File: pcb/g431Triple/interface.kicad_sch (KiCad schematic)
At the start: 29 parts, among them P4 har-flexicon 2,54 MSH-4, P5 har-flexicon 2,54 MSH-4, P6 har-flexicon 2,54 MSH-4, P7 WAGO2061-602, P8 WAGO2061-602, P9 WAGO2061-602, U4 SP3485CN, U5 SP3485CN, U6 SP3485CN

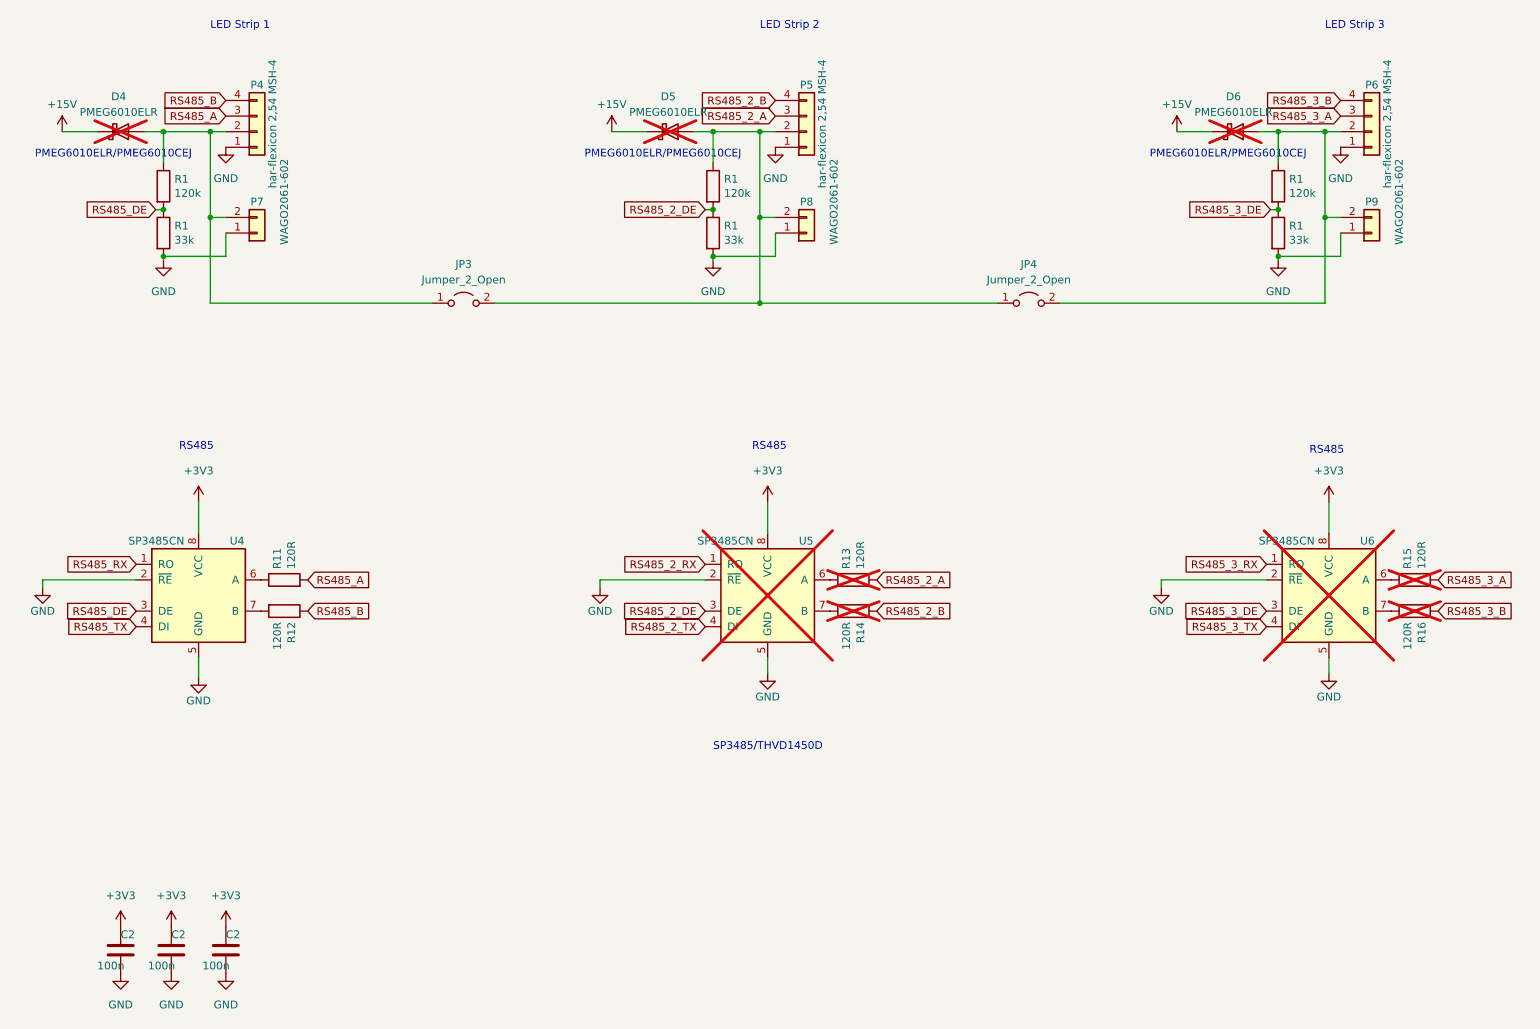
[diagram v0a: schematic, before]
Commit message: Rename to g431/g431Triple, new pin ordering for Harting connector
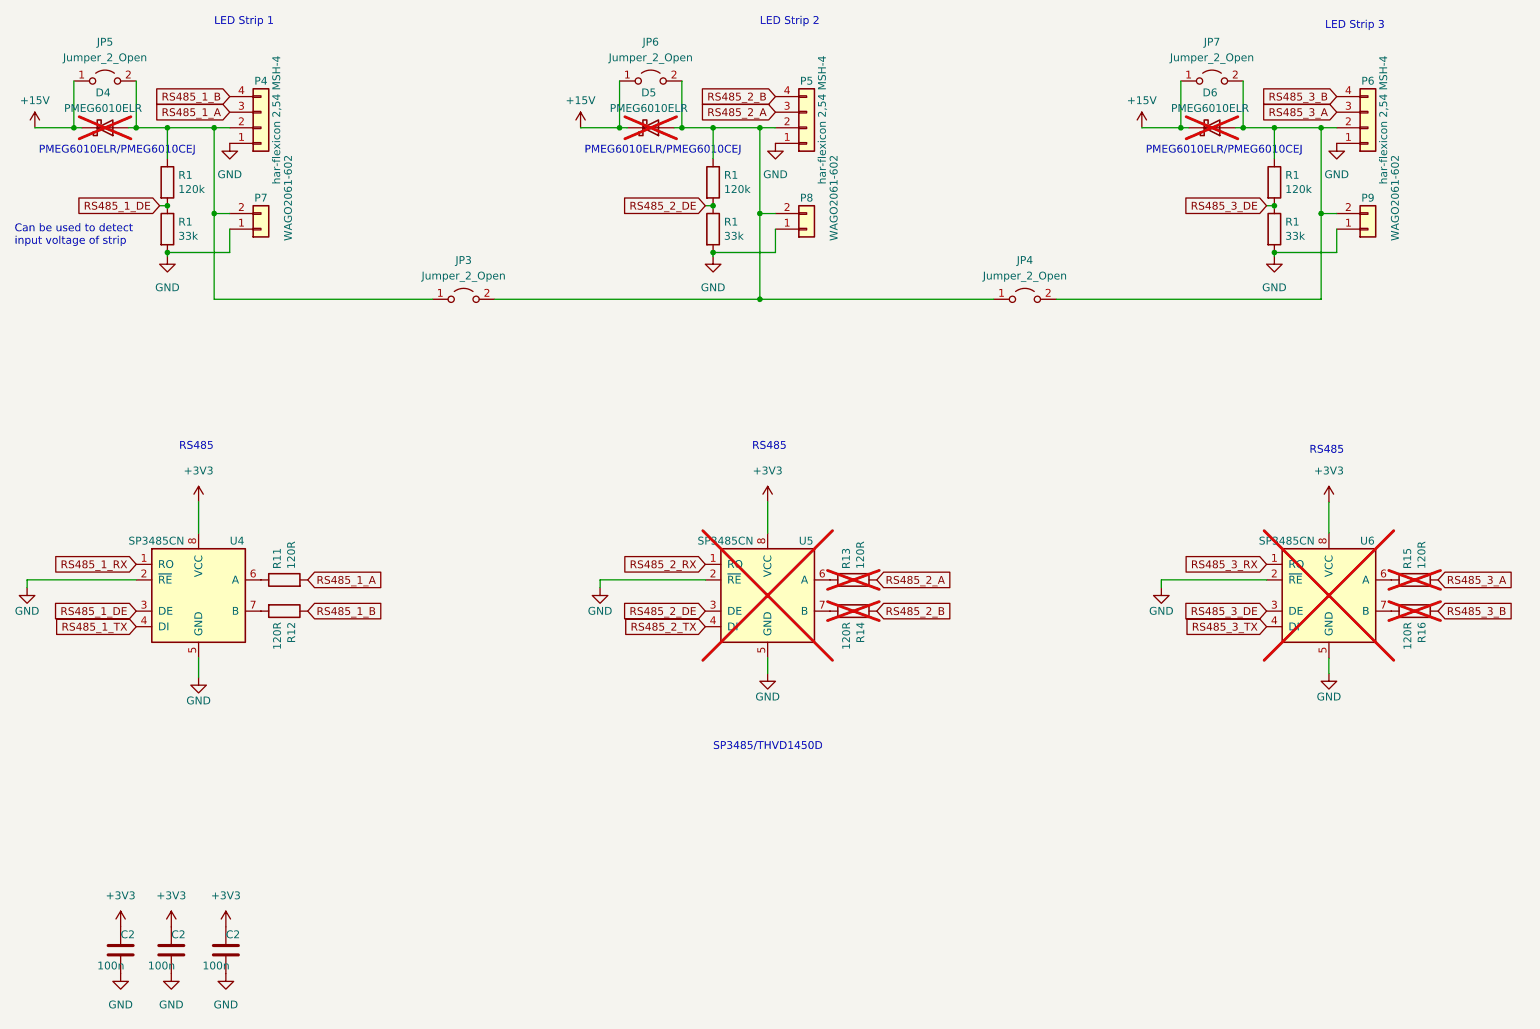
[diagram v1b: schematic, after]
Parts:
- added JP5, JP6, JP7: Jumper_2_Open, local:Jumper, symbol Jumper:Jumper_2_Open
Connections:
- net +15V: now also JP5.1 (A), JP6.1 (A), JP7.1 (A)
- net at D5.2 (A), JP3.2 (B), JP4.1 (A)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: now also JP6.2 (B)
- net at D6.2 (A), JP4.2 (B), P6.2 (Pin_2)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: now also JP7.2 (B)
- net at D4.2 (A), JP3.1 (A), P4.2 (Pin_2)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: now also JP5.2 (B)
- net RS485_A renamed RS485_1_A
- net RS485_B renamed RS485_1_B
- net RS485_DE renamed RS485_1_DE
- net RS485_RX renamed RS485_1_RX
- net RS485_TX renamed RS485_1_TX
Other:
- note added: "Can be used to detect input voltage of strip"
- moved on the sheet: D4, D5, D6, JP3, JP4, P4, P5, P6, P7, P8, P9, R1

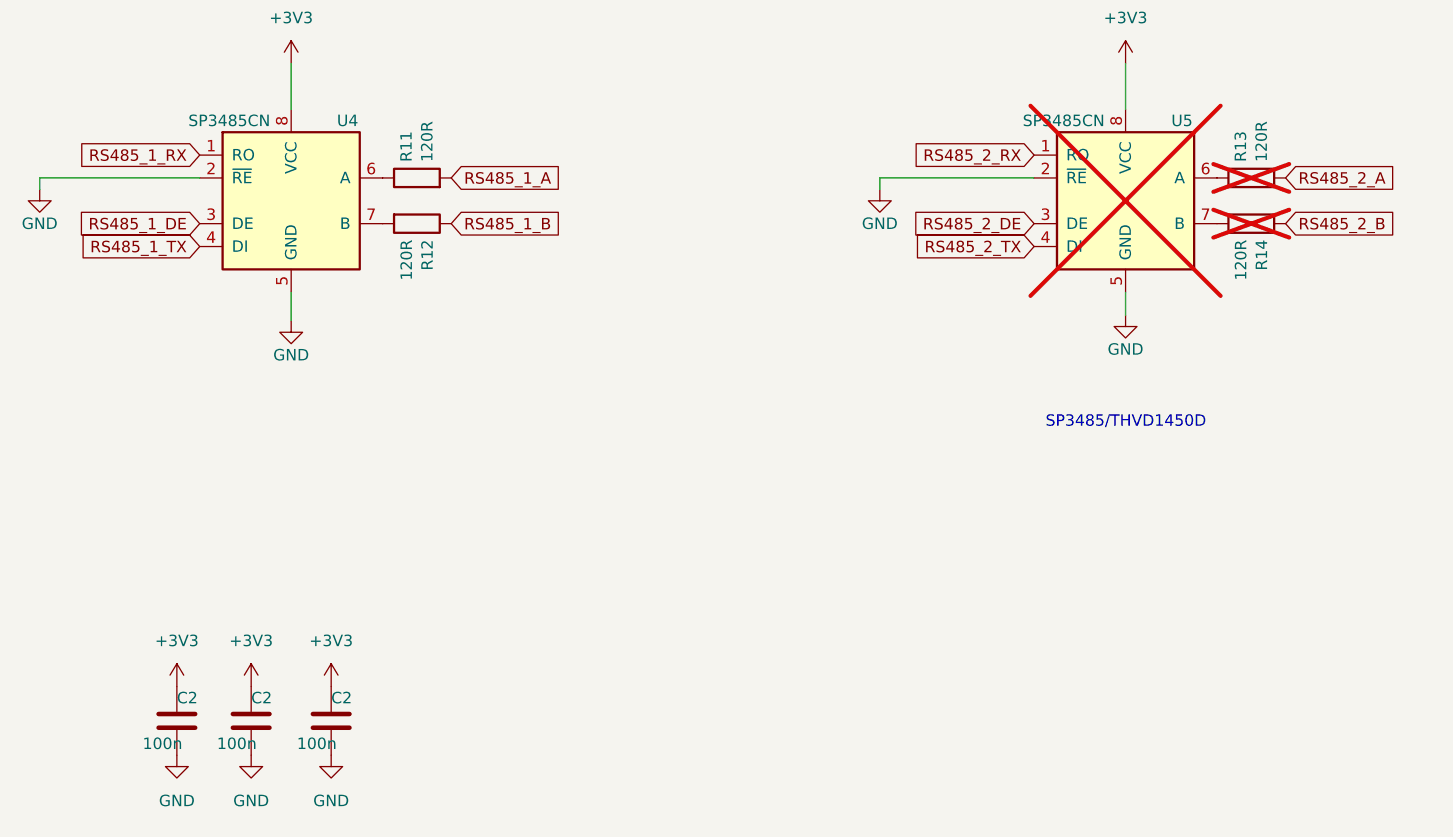
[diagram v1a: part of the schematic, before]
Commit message: Add color temperature
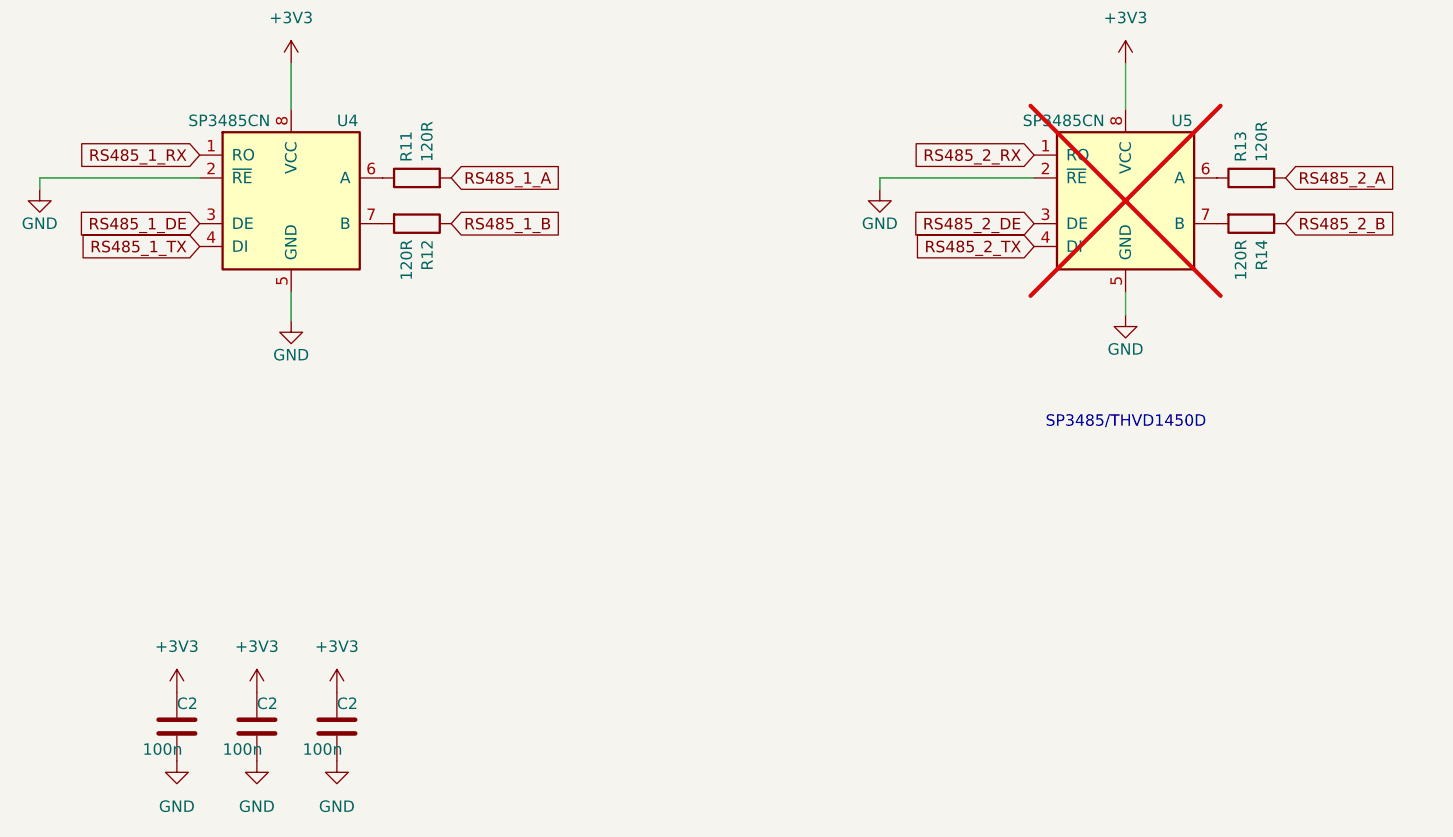
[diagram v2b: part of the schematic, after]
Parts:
- R13, R14: now fitted
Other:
- moved on the sheet: C2
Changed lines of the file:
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@@
 		(in_bom yes)
 		(on_board yes)
-		(dnp yes)
+		(dnp no)
 		(property "Reference" "R14"
 			(at 157.3784 126.238 0)
@@
 		(in_bom yes)
 		(on_board yes)
-		(dnp yes)
+		(dnp no)
 		(property "Reference" "R13"
 			(at 155.0416 117.602 0)
@@
 	(symbol
 		(lib_id "Device:C")
-		(at 45.085 179.705 0)
+		(at 45.72 180.34 0)
 		(unit 1)
 		(exclude_from_sim no)
@@
 		(dnp no)
 		(property "Reference" "C2"
-			(at 45.085 177.165 0)
+			(at 45.72 177.8 0)
 			(effects
 				(font
@@
 		)
 		(property "Value" "100n"
-			(at 41.275 182.245 0)
+			(at 41.91 182.88 0)
 			(effects
 				(font
@@
 		)
 		(property "Footprint" "local:0603"
-			(at 46.0502 183.515 0)
+			(at 46.6852 184.15 0)
 			(effects
 				(font
@@
 		)
 		(property "Datasheet" "~"
-			(at 45.085 179.705 0)
+			(at 45.72 180.34 0)
 			(effects
 				(font
@@
 		)
 		(property "Description" ""
-			(at 45.085 179.705 0)
+			(at 45.72 180.34 0)
 			(effects
 				(font
@@
 			(project "control"
 				(path "/4b540715-c4ed-4902-8525-92fb403f6b2e/20eb032d-dad8-4c28-86ad-cc4f262ed8e2"
-					(reference "C16")
+					(reference "C17")
 					(unit 1)
 				)
@@
 	(symbol
 		(lib_id "power:GND")
-		(at 53.975 183.515 0)
+		(at 54.61 184.15 0)
 		(unit 1)
 		(exclude_from_sim no)
@@
 		(fields_autoplaced yes)
 		(property "Reference" "#PWR010"
-			(at 53.975 189.865 0)
+			(at 54.61 190.5 0)
 			(effects
 				(font
@@
 		)
 		(property "Value" "GND"
-			(at 53.975 188.595 0)
+			(at 54.61 189.23 0)
 			(effects
 				(font
@@
 		)
 		(property "Footprint" ""
-			(at 53.975 183.515 0)
+			(at 54.61 184.15 0)
 			(effects
 				(font
@@
 		)
 		(property "Datasheet" ""
-			(at 53.975 183.515 0)
+			(at 54.61 184.15 0)
 			(effects
 				(font
@@
 		)
 		(property "Description" ""
-			(at 53.975 183.515 0)
+			(at 54.61 184.15 0)
 			(effects
 				(font
@@
 	(symbol
 		(lib_id "Device:C")
-		(at 36.83 179.705 0)
+		(at 36.83 180.34 0)
 		(unit 1)
 		(exclude_from_sim no)
@@
 		(dnp no)
 		(property "Reference" "C2"
-			(at 36.83 177.165 0)
+			(at 36.83 177.8 0)
 			(effects
 				(font
@@
 		)
 		(property "Value" "100n"
-			(at 33.02 182.245 0)
+			(at 33.02 182.88 0)
 			(effects
 				(font
@@
 		)
 		(property "Footprint" "local:0603"
-			(at 37.7952 183.515 0)
+			(at 37.7952 184.15 0)
 			(effects
 				(font
@@
 		)
 		(property "Datasheet" "~"
-			(at 36.83 179.705 0)
+			(at 36.83 180.34 0)
 			(effects
 				(font
@@
 		)
 		(property "Description" ""
-			(at 36.83 179.705 0)
+			(at 36.83 180.34 0)
 			(effects
 				(font
@@
 			(project "control"
 				(path "/4b540715-c4ed-4902-8525-92fb403f6b2e/20eb032d-dad8-4c28-86ad-cc4f262ed8e2"
-					(reference "C15")
+					(reference "C16")
 					(unit 1)
 				)
@@
 	(symbol
 		(lib_id "Device:C")
-		(at 53.975 179.705 0)
+		(at 54.61 180.34 0)
 		(unit 1)
 		(exclude_from_sim no)
@@
 		(dnp no)
 		(property "Reference" "C2"
-			(at 53.975 177.165 0)
+			(at 54.61 177.8 0)
 			(effects
 				(font
@@
 		)
 		(property "Value" "100n"
-			(at 50.165 182.245 0)
+			(at 50.8 182.88 0)
 			(effects
 				(font
@@
 		)
 		(property "Footprint" "local:0603"
-			(at 54.9402 183.515 0)
+			(at 55.5752 184.15 0)
 			(effects
 				(font
@@
 		)
 		(property "Datasheet" "~"
-			(at 53.975 179.705 0)
+			(at 54.61 180.34 0)
 			(effects
 				(font
@@
 		)
 		(property "Description" ""
-			(at 53.975 179.705 0)
+			(at 54.61 180.34 0)
 			(effects
 				(font
@@
 			(project "control"
 				(path "/4b540715-c4ed-4902-8525-92fb403f6b2e/20eb032d-dad8-4c28-86ad-cc4f262ed8e2"
-					(reference "C17")
+					(reference "C18")
 					(unit 1)
 				)
@@
 	(symbol
 		(lib_id "power:+3V3")
-		(at 45.085 175.895 0)
+		(at 45.72 176.53 0)
 		(unit 1)
 		(exclude_from_sim no)
@@
 		(fields_autoplaced yes)
 		(property "Reference" "#PWR09"
-			(at 45.085 179.705 0)
+			(at 45.72 180.34 0)
 			(effects
 				(font
@@
 		)
 		(property "Value" "+3V3"
-			(at 45.085 170.815 0)
+			(at 45.72 171.45 0)
 			(effects
 				(font
@@
 		)
 		(property "Footprint" ""
-			(at 45.085 175.895 0)
+			(at 45.72 176.53 0)
 			(effects
 				(font
@@
 		)
 		(property "Datasheet" ""
-			(at 45.085 175.895 0)
+			(at 45.72 176.53 0)
 			(effects
 				(font
@@
 		)
 		(property "Description" ""
-			(at 45.085 175.895 0)
+			(at 45.72 176.53 0)
 			(effects
 				(font
@@
 	(symbol
 		(lib_id "power:GND")
-		(at 45.085 183.515 0)
+		(at 45.72 184.15 0)
 		(unit 1)
 		(exclude_from_sim no)
@@
 		(fields_autoplaced yes)
 		(property "Reference" "#PWR010"
-			(at 45.085 189.865 0)
+			(at 45.72 190.5 0)
 			(effects
 				(font
@@
 		)
 		(property "Value" "GND"
-			(at 45.085 188.595 0)
+			(at 45.72 189.23 0)
 			(effects
 				(font
@@
 		)
 		(property "Footprint" ""
-			(at 45.085 183.515 0)
+			(at 45.72 184.15 0)
 			(effects
 				(font
@@
 		)
 		(property "Datasheet" ""
-			(at 45.085 183.515 0)
+			(at 45.72 184.15 0)
 			(effects
 				(font
@@
 		)
 		(property "Description" ""
-			(at 45.085 183.515 0)
+			(at 45.72 184.15 0)
 			(effects
 				(font
@@
 	(symbol
 		(lib_id "power:+3V3")
-		(at 36.83 175.895 0)
+		(at 36.83 176.53 0)
 		(unit 1)
 		(exclude_from_sim no)
@@
 		(fields_autoplaced yes)
 		(property "Reference" "#PWR09"
-			(at 36.83 179.705 0)
+			(at 36.83 180.34 0)
 			(effects
 				(font
@@
 		)
 		(property "Value" "+3V3"
-			(at 36.83 170.815 0)
+			(at 36.83 171.45 0)
 			(effects
 				(font
@@
 		)
 		(property "Footprint" ""
-			(at 36.83 175.895 0)
+			(at 36.83 176.53 0)
 			(effects
 				(font
@@
 		)
 		(property "Datasheet" ""
-			(at 36.83 175.895 0)
+			(at 36.83 176.53 0)
 			(effects
 				(font
@@
 		)
 		(property "Description" ""
-			(at 36.83 175.895 0)
+			(at 36.83 176.53 0)
 			(effects
 				(font
@@
 	(symbol
 		(lib_id "power:GND")
-		(at 36.83 183.515 0)
+		(at 36.83 184.15 0)
 		(unit 1)
 		(exclude_from_sim no)
@@
 		(fields_autoplaced yes)
 		(property "Reference" "#PWR010"
-			(at 36.83 189.865 0)
+			(at 36.83 190.5 0)
 			(effects
 				(font
@@
 		)
 		(property "Value" "GND"
-			(at 36.83 188.595 0)
+			(at 36.83 189.23 0)
 			(effects
 				(font
@@
 		)
 		(property "Footprint" ""
-			(at 36.83 183.515 0)
+			(at 36.83 184.15 0)
 			(effects
 				(font
@@
 		)
 		(property "Datasheet" ""
-			(at 36.83 183.515 0)
+			(at 36.83 184.15 0)
 			(effects
 				(font
@@
 		)
 		(property "Description" ""
-			(at 36.83 183.515 0)
+			(at 36.83 184.15 0)
 			(effects
 				(font
@@
 	(symbol
 		(lib_id "power:+3V3")
-		(at 53.975 175.895 0)
+		(at 54.61 176.53 0)
 		(unit 1)
 		(exclude_from_sim no)
@@
 		(fields_autoplaced yes)
 		(property "Reference" "#PWR09"
-			(at 53.975 179.705 0)
+			(at 54.61 180.34 0)
 			(effects
 				(font
@@
 		)
 		(property "Value" "+3V3"
-			(at 53.975 170.815 0)
+			(at 54.61 171.45 0)
 			(effects
 				(font
@@
 		)
 		(property "Footprint" ""
-			(at 53.975 175.895 0)
+			(at 54.61 176.53 0)
 			(effects
 				(font
@@
 		)
 		(property "Datasheet" ""
-			(at 53.975 175.895 0)
+			(at 54.61 176.53 0)
 			(effects
 				(font
@@
 		)
 		(property "Description" ""
-			(at 53.975 175.895 0)
+			(at 54.61 176.53 0)
 			(effects
 				(font
